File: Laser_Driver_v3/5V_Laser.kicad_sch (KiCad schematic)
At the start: 19 parts, among them U14 LM7812_TO220, U15 LM7808_TO220, U16 LT3045EDD 5V, U17 LT3045EDD 5V

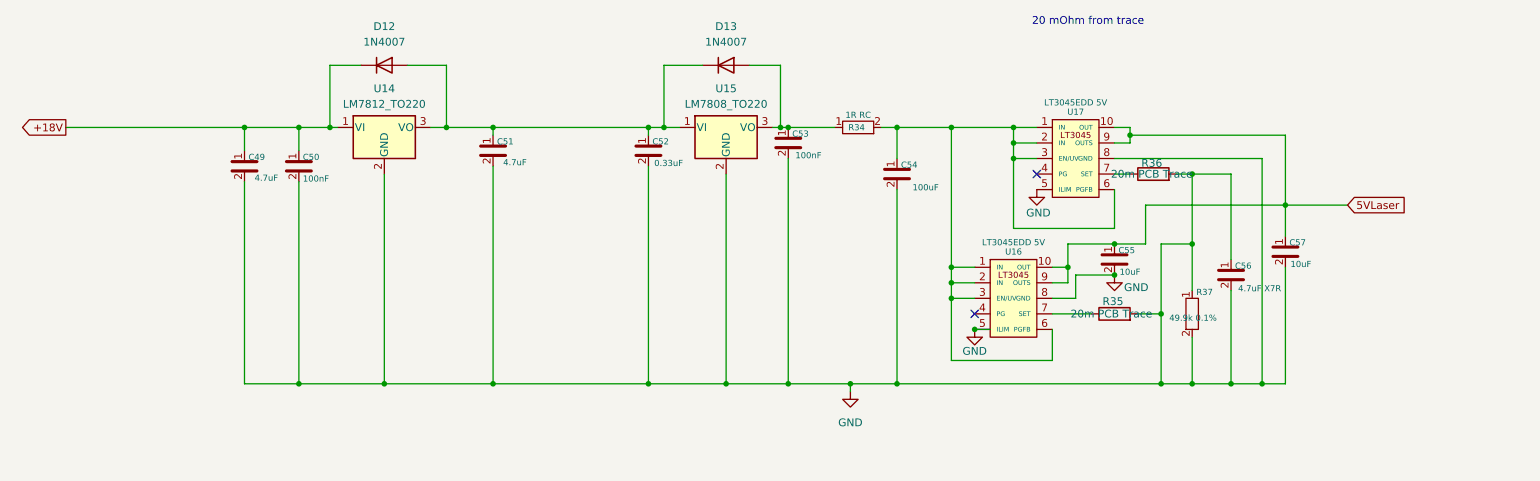
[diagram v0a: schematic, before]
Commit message: Update names, footprints, values, and created BOM
Updated files names, foot prints, component values, parts.
Assigned values from Digikey catalog.
Created CSV BOMs for each schematic.
Including a Power analysis now for all components.
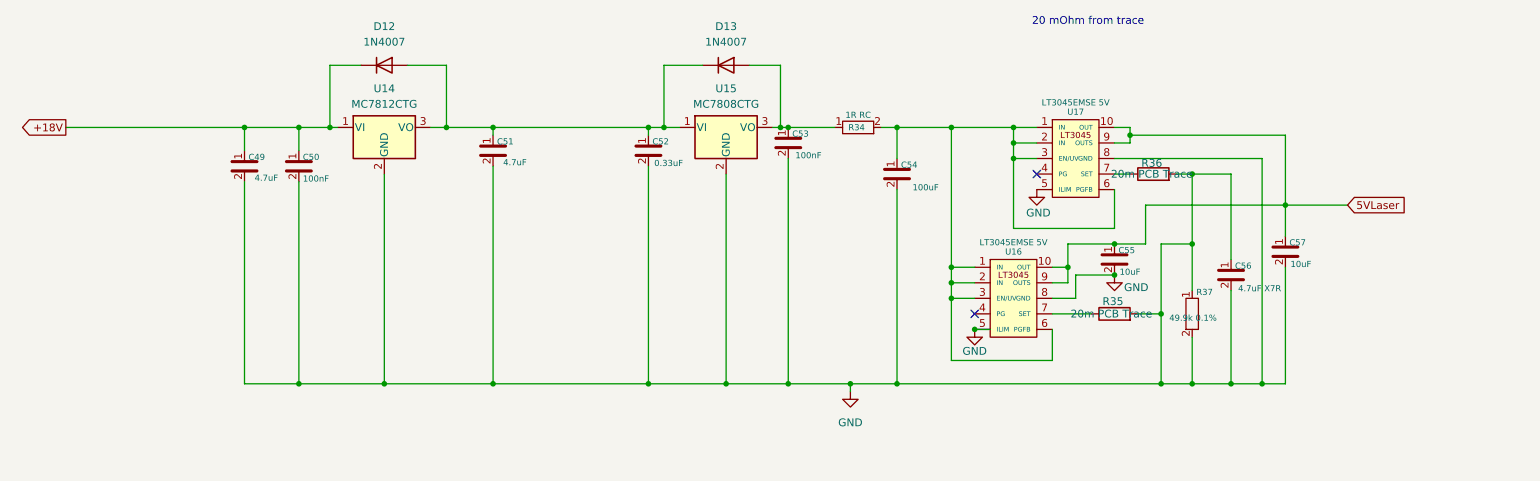
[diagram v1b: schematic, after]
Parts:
- R37: footprint Resistor_SMD:R_0402_1005Metric -> Resistor_SMD:R_0805_2012Metric_Pad1.20x1.40mm_HandSolder
- U14: value LM7812_TO220 -> MC7812CTG
- U15: value LM7808_TO220 -> MC7808CTG
- U16, U17: value LT3045EDD 5V -> LT3045EMSE 5V; footprint Package_DFN_QFN:DFN-10-1EP_3x3mm_P0.5mm_EP1.65x2.38mm -> Package_SO:MSOP-16_3x5mm_P0.65mm
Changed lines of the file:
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@@
 			)
 		)
-		(property "Value" "LM7812_TO220"
+		(property "Value" "MC7812CTG"
 			(at 91.44 38.1 0)
 			(show_name no)
@@
 			)
 		)
-		(property "Value" "LT3045EDD 5V"
+		(property "Value" "LT3045EMSE 5V"
 			(at 194.31 60.706 0)
 			(show_name no)
@@
 			)
 		)
-		(property "Footprint" "Package_DFN_QFN:DFN-10-1EP_3x3mm_P0.5mm_EP1.65x2.38mm"
+		(property "Footprint" "Package_SO:MSOP-16_3x5mm_P0.65mm"
 			(at 114.31 46.58 0)
 			(hide yes)
@@
 			)
 		)
-		(property "Footprint" "Resistor_SMD:R_0402_1005Metric"
+		(property "Footprint" "Resistor_SMD:R_0805_2012Metric_Pad1.20x1.40mm_HandSolder"
 			(at 15.52 40.39 0)
 			(hide yes)
@@
 			)
 		)
-		(property "Value" "LM7808_TO220"
+		(property "Value" "MC7808CTG"
 			(at 147.32 38.1 0)
 			(show_name no)
@@
 			)
 		)
-		(property "Value" "LT3045EDD 5V"
+		(property "Value" "LT3045EMSE 5V"
 			(at 204.47 37.846 0)
 			(show_name no)
@@
 			)
 		)
-		(property "Footprint" "Package_DFN_QFN:DFN-10-1EP_3x3mm_P0.5mm_EP1.65x2.38mm"
+		(property "Footprint" "Package_SO:MSOP-16_3x5mm_P0.65mm"
 			(at 124.47 23.72 0)
 			(hide yes)

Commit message: Update to teensy pinout and config. Working on PCB
Improved pin selection on Teensy for better operation.
Started working through the PCB from in the power input.
Updating footprints and getting the layout organized.
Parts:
- U16, U17: footprint Package_SO:MSOP-16_3x5mm_P0.65mm -> Package_SO:Analog_MSOP-12-16-1EP_3x4.039mm_P0.5mm_EP1.651x2.845mm_ThermalVias
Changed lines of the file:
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@@
 			)
 		)
-		(property "Footprint" "Package_SO:MSOP-16_3x5mm_P0.65mm"
+		(property "Footprint" "Package_SO:Analog_MSOP-12-16-1EP_3x4.039mm_P0.5mm_EP1.651x2.845mm_ThermalVias"
 			(at 114.31 46.58 0)
 			(hide yes)
@@
 			)
 		)
-		(property "Footprint" "Package_SO:MSOP-16_3x5mm_P0.65mm"
+		(property "Footprint" "Package_SO:Analog_MSOP-12-16-1EP_3x4.039mm_P0.5mm_EP1.651x2.845mm_ThermalVias"
 			(at 124.47 23.72 0)
 			(hide yes)

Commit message: Working through power supply layout and footprints
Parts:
- removed U16: LT3045EMSE 5V, Package_SO:Analog_MSOP-12-16-1EP_3x4.039mm_P0.5mm_EP1.651x2.845mm_ThermalVias, symbol Regulator_Linear:LT3042
- added U17: LT3045EMSE 5V, Package_SO:MSOP-12-1EP_3x4.039mm_P0.65mm_EP1.651x2.845mm_ThermalVias, symbol LT3045IMSE_TRPBF:LT3045IMSE_TRPBF
- D12, D13: footprint Diode_THT:D_DO-41_SOD81_P10.16mm_Horizontal -> Diode_THT:D_DO-15_P12.70mm_Horizontal
- U16: renamed from U17; footprint Package_SO:Analog_MSOP-12-16-1EP_3x4.039mm_P0.5mm_EP1.651x2.845mm_ThermalVias -> Package_SO:MSOP-12-1EP_3x4.039mm_P0.65mm_EP1.651x2.845mm_ThermalVias; symbol Regulator_Linear:LT3042 -> LT3045IMSE_TRPBF:LT3045IMSE_TRPBF; Availability (none) -> In Stock; Check_prices (none) -> https://www.snapeda.com/parts/LT3045IMSE%23TRPBF/Analog+Dev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; DUPLICATE (none) -> LT3045HMSE#PBF-,-LT3045EMSE#WPBF-,-LT3045IMSE#WPBF-,-LT3045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; MANUFACTURER (none) -> Analog Devices; MAXIMUM_PACKAGE_HEIGHT (none) -> 1.1mm; MF (none) -> Analog Devices; MP (none) -> LT3045IMSE#TRPBF; PARTREV (none) -> D; Package (none) -> MSOP -12 Analog Devices; Price (none) -> None; Purchase-URL (none) -> https://www.snapeda.com/api/url_track_click_mouser/?unipart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; STANDARD (none) -> IPC-7351B; SnapEDA_Link (none) -> https://www.snapeda.com/parts/LT3045IMSE%23TRPBF/Analog+Dev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
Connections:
- net 5VLaser: now also R35.2, R36.2; no longer C55.1, C57.1, U16.10 (OUT), U16.9 (OUTS)
- net GND: now also U16.13 (EXP), U16.6 (ILIM), U16.9 (GND), U17.13 (EXP), U17.6 (ILIM), U17.9 (GND); no longer C56.1, R35.2, R36.2, R37.1, U16.5 (ILIM), U16.8 (GND)
- net at C54.1, R34.2, U16.1 (IN)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: now also U16.4 (EN/UV), U16.7 (PGFB), U17.1 (IN), U17.2 (IN), U17.3 (IN), U17.4 (EN/UV), U17.7 (PGFB); no longer U16.6 (PGFB)
- net at R35.1: now also C55.1, U17.10 (OUTS), U17.11 (OUT), U17.12 (OUT)
- net at R36.1: now also C57.1, U16.10 (OUTS), U16.11 (OUT), U16.12 (OUT); no longer U16.7 (SET)
- new net: C56.1, R37.1, U16.8 (SET), U17.8 (SET)
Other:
- note removed: "20 mOhm from trace"
- moved on the sheet: C55, C56, C57, R35, R36, R37

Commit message: Added separate xfrmer for 6V.
Added inrush protection with NTC and increased capacitance to reduce ripple on 6V
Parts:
- renumbered C49 to C55, C50 to C56, C51 to C57, C52 to C58, C53 to C59, C54 to C60, C56 to C61, C57 to C62, C55 to C63, R37 to R35, R35 to R37
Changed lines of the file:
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@@
 		(in_pos_files yes)
 		(dnp no)
-		(property "Reference" "C49"
+		(property "Reference" "C55"
 			(at 70.58 46.76 0)
 			(show_name no)
@@
 			(project "laser_driver_v3"
 				(path "/b2c3d4e5-f6a7-8901-bcde-f12345678901/4c904a9b-f13b-4762-ac7d-2743bb4f9a22"
-					(reference "C49")
+					(reference "C55")
 					(unit 1)
 				)
@@
 		(in_pos_files yes)
 		(dnp no)
-		(property "Reference" "R37"
+		(property "Reference" "R35"
 			(at 187.452 67.564 0)
 			(show_name no)
@@
 			(project "laser_driver_v3"
 				(path "/b2c3d4e5-f6a7-8901-bcde-f12345678901/4c904a9b-f13b-4762-ac7d-2743bb4f9a22"
-					(reference "R37")
+					(reference "R35")
 					(unit 1)
 				)
@@
 		(in_pos_files yes)
 		(dnp no)
-		(property "Reference" "R35"
+		(property "Reference" "R37"
 			(at 251.206 70.358 90)
 			(show_name no)
@@
 			(project "laser_driver_v3"
 				(path "/b2c3d4e5-f6a7-8901-bcde-f12345678901/4c904a9b-f13b-4762-ac7d-2743bb4f9a22"
-					(reference "R35")
+					(reference "R37")
 					(unit 1)
 				)
@@
 		(in_pos_files yes)
 		(dnp no)
-		(property "Reference" "#PWR021"
+		(property "Reference" "#PWR018"
 			(at 243.84 55.88 0)
 			(hide yes)
@@
 			(project "laser_driver_v3"
 				(path "/b2c3d4e5-f6a7-8901-bcde-f12345678901/4c904a9b-f13b-4762-ac7d-2743bb4f9a22"
-					(reference "#PWR021")
+					(reference "#PWR018")
 					(unit 1)
 				)
@@
 		(in_pos_files yes)
 		(dnp no)
-		(property "Reference" "C51"
+		(property "Reference" "C57"
 			(at 111.22 44.22 0)
 			(show_name no)
@@
 			(project "laser_driver_v3"
 				(path "/b2c3d4e5-f6a7-8901-bcde-f12345678901/4c904a9b-f13b-4762-ac7d-2743bb4f9a22"
-					(reference "C51")
+					(reference "C57")
 					(unit 1)
 				)
@@
 		(in_pos_files yes)
 		(dnp no)
-		(property "Reference" "C54"
+		(property "Reference" "C60"
 			(at 170.688 48.006 0)
 			(show_name no)
@@
 			(project "laser_driver_v3"
 				(path "/b2c3d4e5-f6a7-8901-bcde-f12345678901/4c904a9b-f13b-4762-ac7d-2743bb4f9a22"
-					(reference "C54")
+					(reference "C60")
 					(unit 1)
 				)
@@
 		(in_pos_files yes)
 		(dnp no)
-		(property "Reference" "#PWR016"
+		(property "Reference" "#PWR019"
 			(at 245.11 87.63 0)
 			(hide yes)
@@
 			(project "laser_driver_v3"
 				(path "/b2c3d4e5-f6a7-8901-bcde-f12345678901/4c904a9b-f13b-4762-ac7d-2743bb4f9a22"
-					(reference "#PWR016")
+					(reference "#PWR019")
 					(unit 1)
 				)
@@
 		(in_pos_files yes)
 		(dnp no)
-		(property "Reference" "C50"
+		(property "Reference" "C56"
 			(at 79.47 46.76 0)
 			(show_name no)
@@
 			(project "laser_driver_v3"
 				(path "/b2c3d4e5-f6a7-8901-bcde-f12345678901/4c904a9b-f13b-4762-ac7d-2743bb4f9a22"
-					(reference "C50")
+					(reference "C56")
 					(unit 1)
 				)
@@
 		(in_pos_files yes)
 		(dnp no)
-		(property "Reference" "#PWR034"
+		(property "Reference" "#PWR017"
 			(at 233.68 99.06 0)
 			(hide yes)
@@
 			(project "laser_driver_v3"
 				(path "/b2c3d4e5-f6a7-8901-bcde-f12345678901/4c904a9b-f13b-4762-ac7d-2743bb4f9a22"
-					(reference "#PWR034")
+					(reference "#PWR017")
 					(unit 1)
 				)
@@
 		(in_pos_files yes)
 		(dnp no)
-		(property "Reference" "C53"
+		(property "Reference" "C59"
 			(at 159.48 42.95 0)
 			(show_name no)
@@
 			(project "laser_driver_v3"
 				(path "/b2c3d4e5-f6a7-8901-bcde-f12345678901/4c904a9b-f13b-4762-ac7d-2743bb4f9a22"
-					(reference "C53")
+					(reference "C59")
 					(unit 1)
 				)
@@
 		(in_pos_files yes)
 		(dnp no)
-		(property "Reference" "C52"
+		(property "Reference" "C58"
 			(at 136.62 44.22 0)
 			(show_name no)
@@
 			(project "laser_driver_v3"
 				(path "/b2c3d4e5-f6a7-8901-bcde-f12345678901/4c904a9b-f13b-4762-ac7d-2743bb4f9a22"
-					(reference "C52")
+					(reference "C58")
 					(unit 1)
 				)
@@
 		(in_pos_files yes)
 		(dnp no)
-		(property "Reference" "C56"
+		(property "Reference" "C61"
 			(at 193.802 70.358 0)
 			(show_name no)
@@
 			(project "laser_driver_v3"
 				(path "/b2c3d4e5-f6a7-8901-bcde-f12345678901/4c904a9b-f13b-4762-ac7d-2743bb4f9a22"
-					(reference "C56")
+					(reference "C61")
 					(unit 1)
 				)
@@
 		(in_pos_files yes)
 		(dnp no)
-		(property "Reference" "C57"
+		(property "Reference" "C62"
 			(at 245.84 42.95 0)
 			(show_name no)
@@
 			(project "laser_driver_v3"
 				(path "/b2c3d4e5-f6a7-8901-bcde-f12345678901/4c904a9b-f13b-4762-ac7d-2743bb4f9a22"
-					(reference "C57")
+					(reference "C62")
 					(unit 1)
 				)
@@
 		(in_pos_files yes)
 		(dnp no)
-		(property "Reference" "#PWR033"
+		(property "Reference" "#PWR016"
 			(at 233.68 68.58 0)
 			(hide yes)
@@
 			(project "laser_driver_v3"
 				(path "/b2c3d4e5-f6a7-8901-bcde-f12345678901/4c904a9b-f13b-4762-ac7d-2743bb4f9a22"
-					(reference "#PWR033")
+					(reference "#PWR016")
 					(unit 1)
 				)
@@
 		(in_pos_files yes)
 		(dnp no)
-		(property "Reference" "C55"
+		(property "Reference" "C63"
 			(at 247.11 74.7 0)
 			(show_name no)
@@
 			(project "laser_driver_v3"
 				(path "/b2c3d4e5-f6a7-8901-bcde-f12345678901/4c904a9b-f13b-4762-ac7d-2743bb4f9a22"
-					(reference "C55")
+					(reference "C63")
 					(unit 1)
 				)
@@
 		(dnp no)
 		(fields_autoplaced yes)
-		(property "Reference" "#PWR013"
+		(property "Reference" "#PWR015"
 			(at 167.64 91.44 0)
 			(hide yes)
@@
 			(project "laser_driver_v3"
 				(path "/b2c3d4e5-f6a7-8901-bcde-f12345678901/4c904a9b-f13b-4762-ac7d-2743bb4f9a22"
-					(reference "#PWR013")
-					(unit 1)
-				)
+					(reference "#PWR015")
+					(unit 1)
+				)

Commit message: Changed xfrmers, paralled BJTs for cap multiplier
Changed the transformers to more appropriate voltages.
Made the BJTs for the cap multipliers in parallel to better handle the load.
Simulated the output ripple for the 6V.
Clarifying notes, removed LT1028 changed to OPA192 to match circuit as drawn.
Changed divider values for the TEC_zero value to be 1.2 V as designed.
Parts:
- renumbered R34 to R36, R35 to R37, R36 to R38, R37 to R39
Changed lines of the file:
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@@
 		(in_pos_files yes)
 		(dnp no)
-		(property "Reference" "R35"
+		(property "Reference" "R37"
 			(at 187.452 67.564 0)
 			(show_name no)
@@
 			(project "laser_driver_v3"
 				(path "/b2c3d4e5-f6a7-8901-bcde-f12345678901/4c904a9b-f13b-4762-ac7d-2743bb4f9a22"
-					(reference "R35")
+					(reference "R37")
 					(unit 1)
 				)
@@
 		(in_pos_files yes)
 		(dnp no)
-		(property "Reference" "R37"
+		(property "Reference" "R39"
 			(at 251.206 70.358 90)
 			(show_name no)
@@
 			(project "laser_driver_v3"
 				(path "/b2c3d4e5-f6a7-8901-bcde-f12345678901/4c904a9b-f13b-4762-ac7d-2743bb4f9a22"
-					(reference "R37")
+					(reference "R39")
 					(unit 1)
 				)
@@
 		(in_pos_files yes)
 		(dnp no)
-		(property "Reference" "R36"
+		(property "Reference" "R38"
 			(at 251.206 40.132 90)
 			(show_name no)
@@
 			(project "laser_driver_v3"
 				(path "/b2c3d4e5-f6a7-8901-bcde-f12345678901/4c904a9b-f13b-4762-ac7d-2743bb4f9a22"
-					(reference "R36")
+					(reference "R38")
 					(unit 1)
 				)
@@
 		(in_pos_files yes)
 		(dnp no)
-		(property "Reference" "R34"
+		(property "Reference" "R36"
 			(at 168.656 41.91 90)
 			(show_name no)
@@
 			(project "laser_driver_v3"
 				(path "/b2c3d4e5-f6a7-8901-bcde-f12345678901/4c904a9b-f13b-4762-ac7d-2743bb4f9a22"
-					(reference "R34")
-					(unit 1)
-				)
+					(reference "R36")
+					(unit 1)
+				)

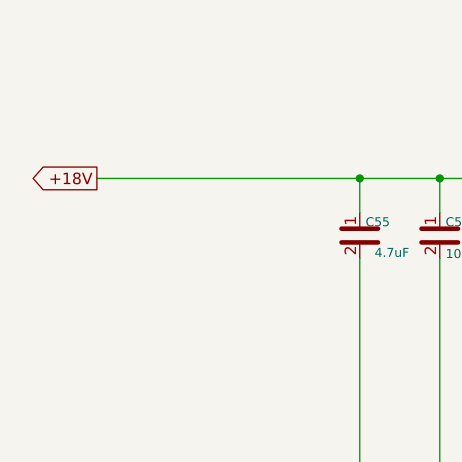
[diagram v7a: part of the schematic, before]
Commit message: Many changes.  Working through ERC.
Main changes are for the grounds.  I found the NETTIE function to tie the GND, DGND and AGND together at a specific point on the boud with a footprint even.
Changed transformers one more time to be consistent for both.
Updated footprints to be consistent and avoid power input/output errors with the ERC.
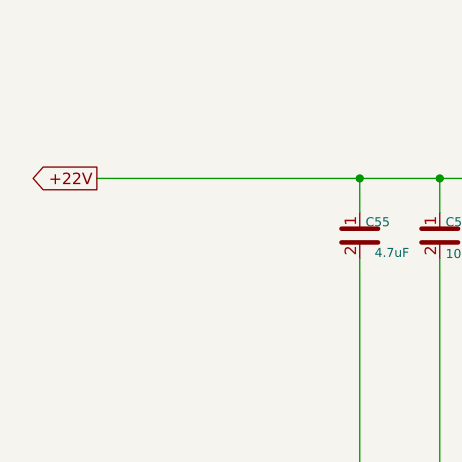
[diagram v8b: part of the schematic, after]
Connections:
- net +18V renamed +22V
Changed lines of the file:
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@@
 		)
 	)
-	(global_label "+18V"
+	(global_label "+22V"
 		(shape output)
 		(at 39.37 41.91 180)
@@
 	)
 	(symbol
+		(lib_name "LT3045IMSE_TRPBF_1")
 		(lib_id "LT3045IMSE_TRPBF:LT3045IMSE_TRPBF")
 		(at 215.9 52.07 0)
